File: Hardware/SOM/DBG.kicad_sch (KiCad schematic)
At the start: 0 parts

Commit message: DDR Banks Vref
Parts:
- added R1, R2, R24, R25, R3: 10K, Resistor_SMD:R_0402_1005Metric, symbol Device:R
- added R20, R21, R22, R23: 4.7k, Resistor_SMD:R_0402_1005Metric, symbol Device:R
- added U1: LFE5UM5G-85F, Package_BGA:Lattice_caBGA-381_17x17mm_Layout20x20_P0.8mm, symbol FPGA_Lattice:LFE5UM5G-85F-8BG381x
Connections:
- new net 3.3V: R1.1, R20.2, R21.2, R22.2, R24.1, R25.1
- new net BOOT_MODE_0: R3.2, U1.U4 (CFG_0)
- new net BOOT_MODE_1: R1.2, U1.T4 (CFG_1)
- new net BOOT_MODE_2: R2.2, U1.R4 (CFG_2)
- new net DONE: U1.Y3 (DONE)
- new net GND: R2.1, R23.2, R3.1
- new net INIT#: R25.2, U1.V3 (~{INIT})
- new net JTAG_TCK: R23.1, U1.T5 (TCK)
- new net JTAG_TDI: R21.1, U1.R5 (TDI)
- new net JTAG_TDO: R20.1, U1.V4 (TDO)
- new net JTAG_TMS: R22.1, U1.U5 (TMS)
- new net PROGRAM#: R24.2, U1.W3 (~{PROGRAM})
- new net QSPI_CLK: U1.U3 (CCLK)
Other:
- note added: "FPGA: DEBUG"
- note added: "ON CARRIER BOARD"
- note added: "REF.: FPGA-EB-02017-1.3"
- note added: "RESISTORS MAY BE PLACED"

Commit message: SOM: power supplies
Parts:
- added R26: 10K, Resistor_SMD:R_0402_1005Metric, symbol Device:R
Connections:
- net 3.3V: now also R26.1
- net DONE: now also R26.2
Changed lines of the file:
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@@
 	)
 	(junction
+		(at 27.94 41.91)
+		(diameter 0)
+		(color 0 0 0 0)
+	)
+	(junction
 		(at 88.9 36.83)
 		(diameter 0)
@@
 	)
 	(junction
+		(at 46.99 41.91)
+		(diameter 0)
+		(color 0 0 0 0)
+	)
+	(junction
 		(at 48.26 59.69)
 		(diameter 0)
@@
 	(wire
 		(pts
-			(xy 27.94 39.37) (xy 27.94 49.53)
+			(xy 27.94 39.37) (xy 27.94 41.91)
 		)
 		(stroke
@@
 	(wire
 		(pts
+			(xy 27.94 41.91) (xy 31.75 41.91)
+		)
+		(stroke
+			(width 0)
+			(type default)
+		)
+	)
+	(wire
+		(pts
 			(xy 50.8 57.15) (xy 50.8 54.61)
 		)
@@
 	(wire
 		(pts
+			(xy 27.94 41.91) (xy 27.94 49.53)
+		)
+		(stroke
+			(width 0)
+			(type default)
+		)
+	)
+	(wire
+		(pts
+			(xy 39.37 41.91) (xy 46.99 41.91)
+		)
+		(stroke
+			(width 0)
+			(type default)
+		)
+	)
+	(wire
+		(pts
 			(xy 39.37 59.69) (xy 48.26 59.69)
 		)
@@
 					(unit 1)
 				)
+			)
+		)
+	)
+	(symbol
+		(lib_id "Device:R")
+		(at 35.56 41.91 90)
+		(unit 1)
+		(exclude_from_sim no)
+		(in_bom yes)
+		(on_board yes)
+		(dnp no)
+		(property "Reference" "R26"
+			(at 33.02 40.894 90)
+			(effects
+				(font
+					(size 1.27 1.27)
+				)
+				(justify left)
+			)
+		)
+		(property "Value" "10K"
+			(at 42.164 40.894 90)
+			(effects
+				(font
+					(size 1.27 1.27)
+				)
+				(justify left)
+			)
+		)
+		(property "Footprint" "Resistor_SMD:R_0402_1005Metric"
+			(at 35.56 43.688 90)
+			(effects
+				(font
+					(size 1.27 1.27)
+				)
+				(hide yes)
+			)
+		)
+		(property "Datasheet" "~"
+			(at 35.56 41.91 0)
+			(effects
+				(font
+					(size 1.27 1.27)
+				)
+				(hide yes)
+			)
+		)
+		(property "Description" "Resistor"
+			(at 35.56 41.91 0)
+			(effects
+				(font
+					(size 1.27 1.27)
+				)
+				(hide yes)
+			)
+		)
+		(property "Manufacturer" "Würth Elektronik"
+			(at 35.56 41.91 0)
+			(effects
+				(font
+					(size 1.27 1.27)
+				)
+				(hide yes)
+			)
+		)
+		(property "MPN" "560112110020"
+			(at 35.56 41.91 0)
+			(effects
+				(font
+					(size 1.27 1.27)
+				)
+				(hide yes)
+			)
+		)
+		(pin "1"
+		)
+		(pin "2"
+		)
+		(instances
+			(project "LFE5UM5G-85F_SOM"
+				(path "/de32abb0-ff3b-4c67-a91a-eed08140b1b2/43f6cb83-1191-4b95-bd87-2dcb3953d05b"
+					(reference "R26")
+					(unit 1)
+				)

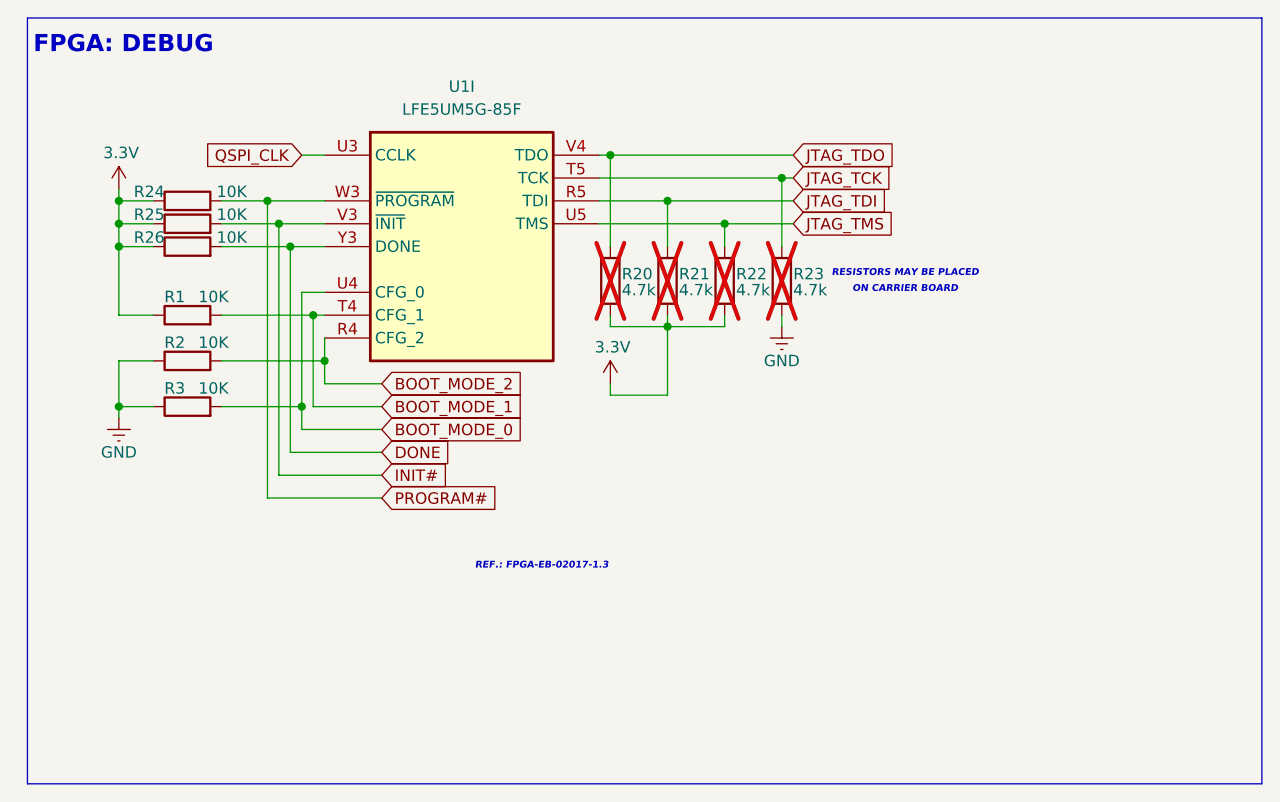
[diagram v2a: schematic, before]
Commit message: SOM: power supply update
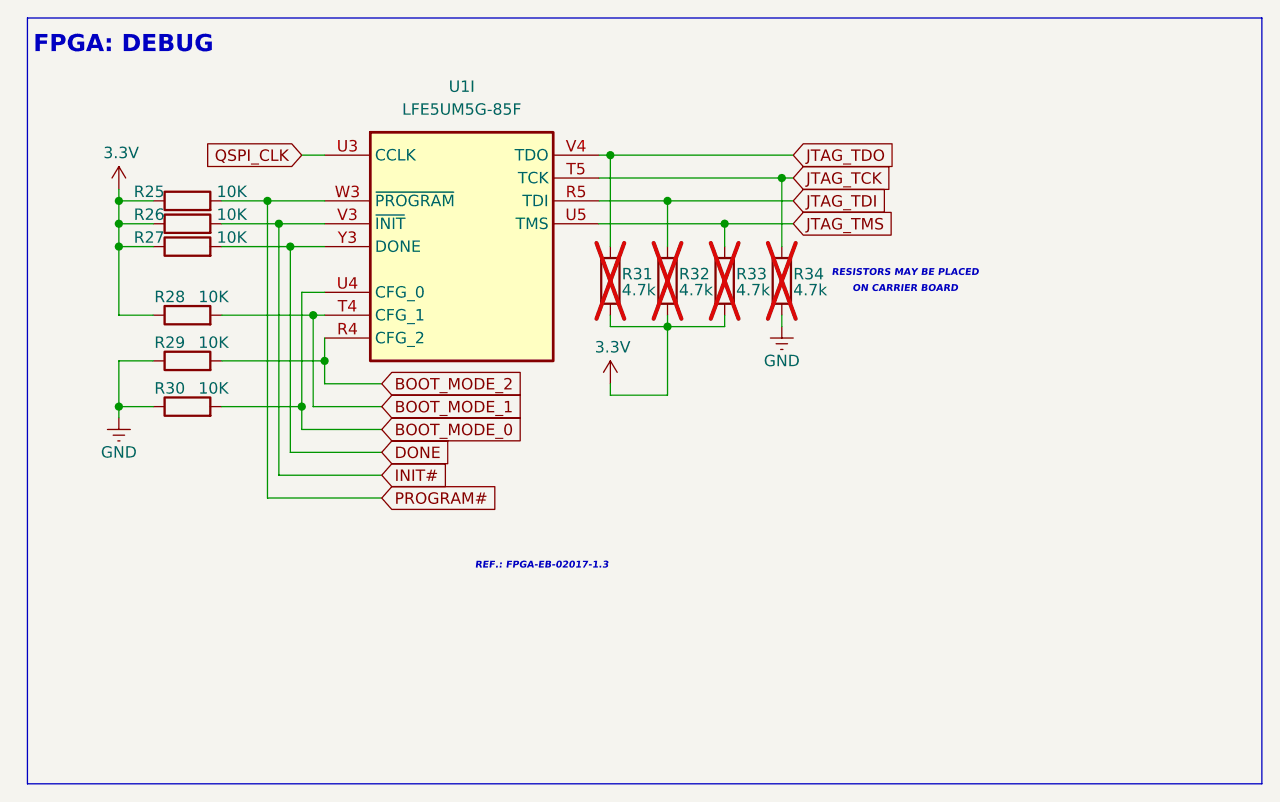
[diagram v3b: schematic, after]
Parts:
- renumbered R24 to R25, R25 to R26, R26 to R27, R1 to R28, R2 to R29, R3 to R30, R20 to R31, R21 to R32, R22 to R33, R23 to R34
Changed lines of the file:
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@@
 		(on_board yes)
 		(dnp no)
-		(property "Reference" "R3"
+		(property "Reference" "R30"
 			(at 35.306 57.658 90)
 			(effects
@@
 			(project "LFE5UM5G-85F_SOM"
 				(path "/de32abb0-ff3b-4c67-a91a-eed08140b1b2/43f6cb83-1191-4b95-bd87-2dcb3953d05b"
-					(reference "R3")
+					(reference "R30")
 					(unit 1)
 				)
@@
 		(on_board yes)
 		(dnp no)
-		(property "Reference" "#PWR041"
+		(property "Reference" "#PWR073"
 			(at 101.6 57.15 0)
 			(effects
@@
 			(project "LFE5UM5G-85F_SOM"
 				(path "/de32abb0-ff3b-4c67-a91a-eed08140b1b2/43f6cb83-1191-4b95-bd87-2dcb3953d05b"
-					(reference "#PWR041")
+					(reference "#PWR073")
 					(unit 1)
 				)
@@
 		(on_board yes)
 		(dnp no)
-		(property "Reference" "R24"
+		(property "Reference" "R25"
 			(at 33.02 35.814 90)
 			(effects
@@
 			(project "LFE5UM5G-85F_SOM"
 				(path "/de32abb0-ff3b-4c67-a91a-eed08140b1b2/43f6cb83-1191-4b95-bd87-2dcb3953d05b"
-					(reference "R24")
+					(reference "R25")
 					(unit 1)
 				)
@@
 		(on_board yes)
 		(dnp yes)
-		(property "Reference" "R22"
+		(property "Reference" "R33"
 			(at 96.52 44.958 0)
 			(effects
@@
 			(project "LFE5UM5G-85F_SOM"
 				(path "/de32abb0-ff3b-4c67-a91a-eed08140b1b2/43f6cb83-1191-4b95-bd87-2dcb3953d05b"
-					(reference "R22")
+					(reference "R33")
 					(unit 1)
 				)
@@
 		(on_board yes)
 		(dnp no)
-		(property "Reference" "R1"
+		(property "Reference" "R28"
 			(at 35.306 47.498 90)
 			(effects
@@
 			(project "LFE5UM5G-85F_SOM"
 				(path "/de32abb0-ff3b-4c67-a91a-eed08140b1b2/43f6cb83-1191-4b95-bd87-2dcb3953d05b"
-					(reference "R1")
+					(reference "R28")
 					(unit 1)
 				)
@@
 		(on_board yes)
 		(dnp no)
-		(property "Reference" "#PWR021"
+		(property "Reference" "#PWR071"
 			(at 27.94 67.31 0)
 			(effects
@@
 			(project "LFE5UM5G-85F_SOM"
 				(path "/de32abb0-ff3b-4c67-a91a-eed08140b1b2/43f6cb83-1191-4b95-bd87-2dcb3953d05b"
-					(reference "#PWR021")
+					(reference "#PWR071")
 					(unit 1)
 				)
@@
 		(on_board yes)
 		(dnp yes)
-		(property "Reference" "R21"
+		(property "Reference" "R32"
 			(at 90.17 44.958 0)
 			(effects
@@
 			(project "LFE5UM5G-85F_SOM"
 				(path "/de32abb0-ff3b-4c67-a91a-eed08140b1b2/43f6cb83-1191-4b95-bd87-2dcb3953d05b"
-					(reference "R21")
+					(reference "R32")
 					(unit 1)
 				)
@@
 		(on_board yes)
 		(dnp no)
-		(property "Reference" "R25"
+		(property "Reference" "R26"
 			(at 33.02 38.354 90)
 			(effects
@@
 			(project "LFE5UM5G-85F_SOM"
 				(path "/de32abb0-ff3b-4c67-a91a-eed08140b1b2/43f6cb83-1191-4b95-bd87-2dcb3953d05b"
-					(reference "R25")
+					(reference "R26")
 					(unit 1)
 				)
@@
 		(on_board yes)
 		(dnp yes)
-		(property "Reference" "R23"
+		(property "Reference" "R34"
 			(at 102.87 44.958 0)
 			(effects
@@
 			(project "LFE5UM5G-85F_SOM"
 				(path "/de32abb0-ff3b-4c67-a91a-eed08140b1b2/43f6cb83-1191-4b95-bd87-2dcb3953d05b"
-					(reference "R23")
+					(reference "R34")
 					(unit 1)
 				)
@@
 		(on_board yes)
 		(dnp no)
-		(property "Reference" "#PWR042"
+		(property "Reference" "#PWR072"
 			(at 82.55 60.96 0)
 			(effects
@@
 			(project "LFE5UM5G-85F_SOM"
 				(path "/de32abb0-ff3b-4c67-a91a-eed08140b1b2/43f6cb83-1191-4b95-bd87-2dcb3953d05b"
-					(reference "#PWR042")
+					(reference "#PWR072")
 					(unit 1)
 				)
@@
 		(on_board yes)
 		(dnp no)
-		(property "Reference" "#PWR020"
+		(property "Reference" "#PWR070"
 			(at 27.94 39.37 0)
 			(effects
@@
 			(project "LFE5UM5G-85F_SOM"
 				(path "/de32abb0-ff3b-4c67-a91a-eed08140b1b2/43f6cb83-1191-4b95-bd87-2dcb3953d05b"
-					(reference "#PWR020")
+					(reference "#PWR070")
 					(unit 1)
 				)
@@
 		(on_board yes)
 		(dnp yes)
-		(property "Reference" "R20"
+		(property "Reference" "R31"
 			(at 83.82 44.958 0)
 			(effects
@@
 			(project "LFE5UM5G-85F_SOM"
 				(path "/de32abb0-ff3b-4c67-a91a-eed08140b1b2/43f6cb83-1191-4b95-bd87-2dcb3953d05b"
-					(reference "R20")
+					(reference "R31")
 					(unit 1)
 				)
@@
 		(on_board yes)
 		(dnp no)
-		(property "Reference" "R2"
+		(property "Reference" "R29"
 			(at 35.306 52.578 90)
 			(effects
@@
 			(project "LFE5UM5G-85F_SOM"
 				(path "/de32abb0-ff3b-4c67-a91a-eed08140b1b2/43f6cb83-1191-4b95-bd87-2dcb3953d05b"
-					(reference "R2")
+					(reference "R29")
 					(unit 1)
 				)
@@
 		(on_board yes)
 		(dnp no)
-		(property "Reference" "R26"
+		(property "Reference" "R27"
 			(at 33.02 40.894 90)
 			(effects
@@
 			(project "LFE5UM5G-85F_SOM"
 				(path "/de32abb0-ff3b-4c67-a91a-eed08140b1b2/43f6cb83-1191-4b95-bd87-2dcb3953d05b"
-					(reference "R26")
+					(reference "R27")
 					(unit 1)
 				)

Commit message: DDR reconnect
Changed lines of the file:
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@@
 	(rectangle
 		(start 17.78 16.51)
-		(end 154.94 101.6)
+		(end 126.746 101.6)
 		(stroke
 			(width 0)
